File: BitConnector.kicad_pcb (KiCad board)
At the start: 2 copper layers, 21.1 x 53.3 mm, 24 parts, among them J1 JTAG, J1 disable_schmitt_trigger_action, J2 Conn_01x02, SW1 reset, U1 XC95##XL-VQ44, U2 74LVC2G14

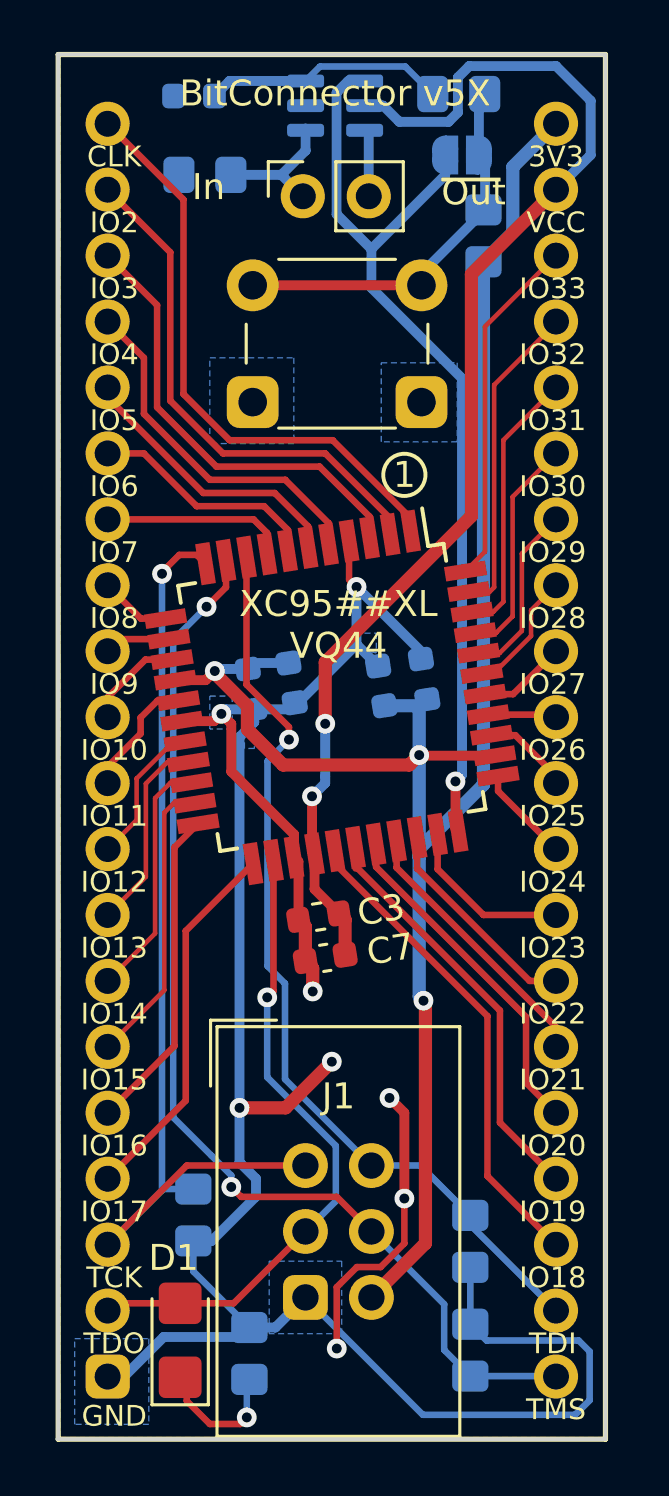
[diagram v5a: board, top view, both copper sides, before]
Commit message: Test circuit with improved GND connection connection
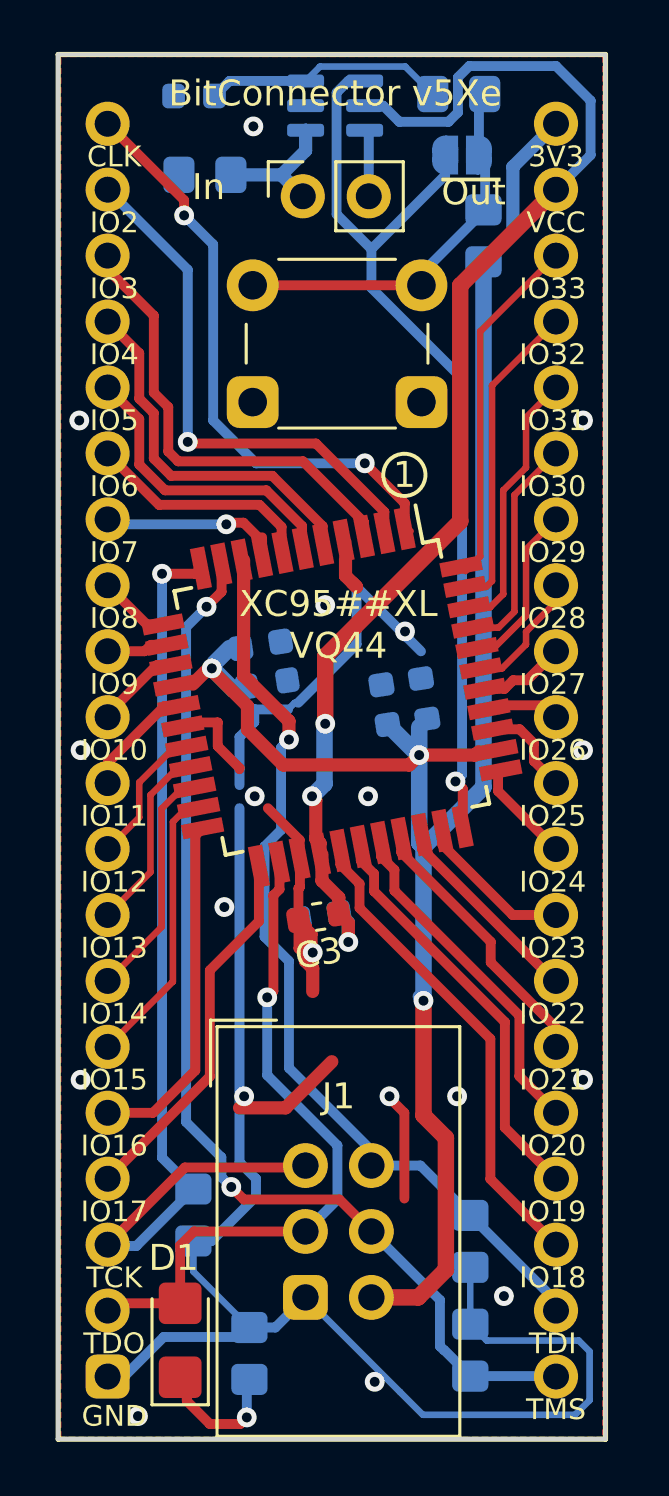
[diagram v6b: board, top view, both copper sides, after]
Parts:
- removed the G*** at (169.4, 103.2)
- added G***: LOGO, logo:logo3, B.Cu at (169.9, 104.5)
- C7: moved to B.Cu
- moved C5 1.89 mm to (167.1, 94.5), turned to 9 degrees
- moved C7 1.62 mm to (169.3, 104.9)
- moved C2 0.75 mm to (173.4, 96.6)
- moved C6 0.73 mm to (171.8, 96.8)
- moved C1 0.66 mm to (167.3, 96.0), turned to 9 degrees
- turned U1 to 281 degrees
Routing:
- net GND: track 105.7 -> 94.0 mm, vias 8 -> 19
- net /GP_IO_10: track 4.75 -> 3.33 mm
- net /JTAG_TDO: track 25.6 -> 27.0 mm
- net /GP_IO_16: track 12.6 -> 13.5 mm
- net /GP_IO_19: track 16.8 -> 15.9 mm
- net VCC: track 49.1 -> 49.9 mm, vias 2 -> 3
- net /GP_IO_20: track 13.9 -> 13.2 mm
- net /GP_IO_5: track 11.0 -> 11.6 mm
- net /GP_IO_23: track 6.63 -> 6.04 mm
- net /GP_IO_7: track 7.17 -> 7.69 mm, vias 0 -> 1
- net /GP_IO_2: track 20.1 -> 20.6 mm, vias 0 -> 1
- net /GP_IO_4: track 13.8 -> 14.3 mm
- net /CLK_GP_IO_1: vias 0 -> 2
- added copper zone on F.Cu, net GND
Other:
- board text added: "BitConnector v5Xe"
- board text removed: "BitConnector v5X"

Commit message: Optimize the distance between the two pin headers
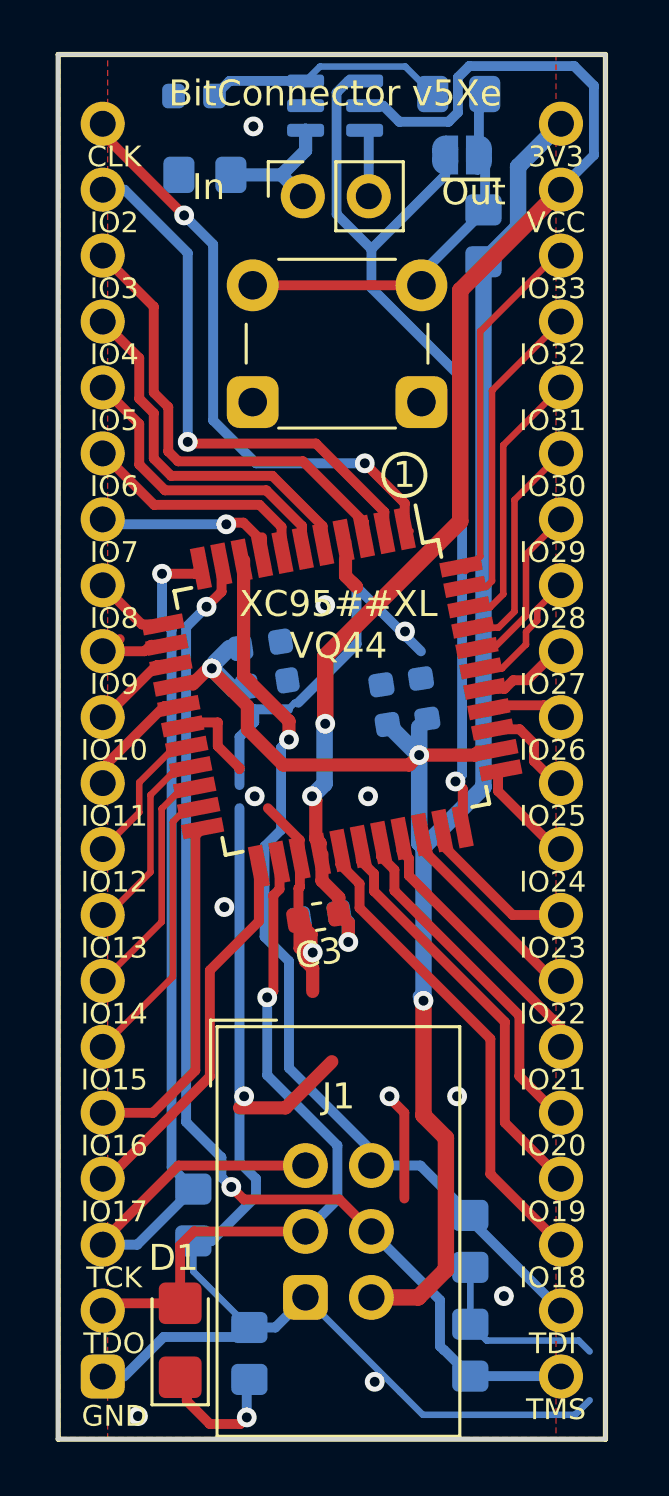
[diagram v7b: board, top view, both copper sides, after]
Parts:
- moved DIP_20_l1 0.19 mm to (161.0, 74.4)
- moved DIP_20_r1 0.19 mm to (178.6, 74.4)
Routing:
- net GND: track 94.0 -> 92.1 mm, vias 19 -> 13
- net +3V3: track 76.7 -> 75.4 mm
- net /GP_IO_28: track 4.88 -> 5.59 mm
- net /GP_IO_3: track 17.7 -> 18.3 mm
- net /JTAG_TCK: track 39.0 -> 39.6 mm
- net /GP_IO_2: track 20.6 -> 21.2 mm
- net VCC: track 49.9 -> 50.4 mm

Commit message: Revise the concept of PCB labeling
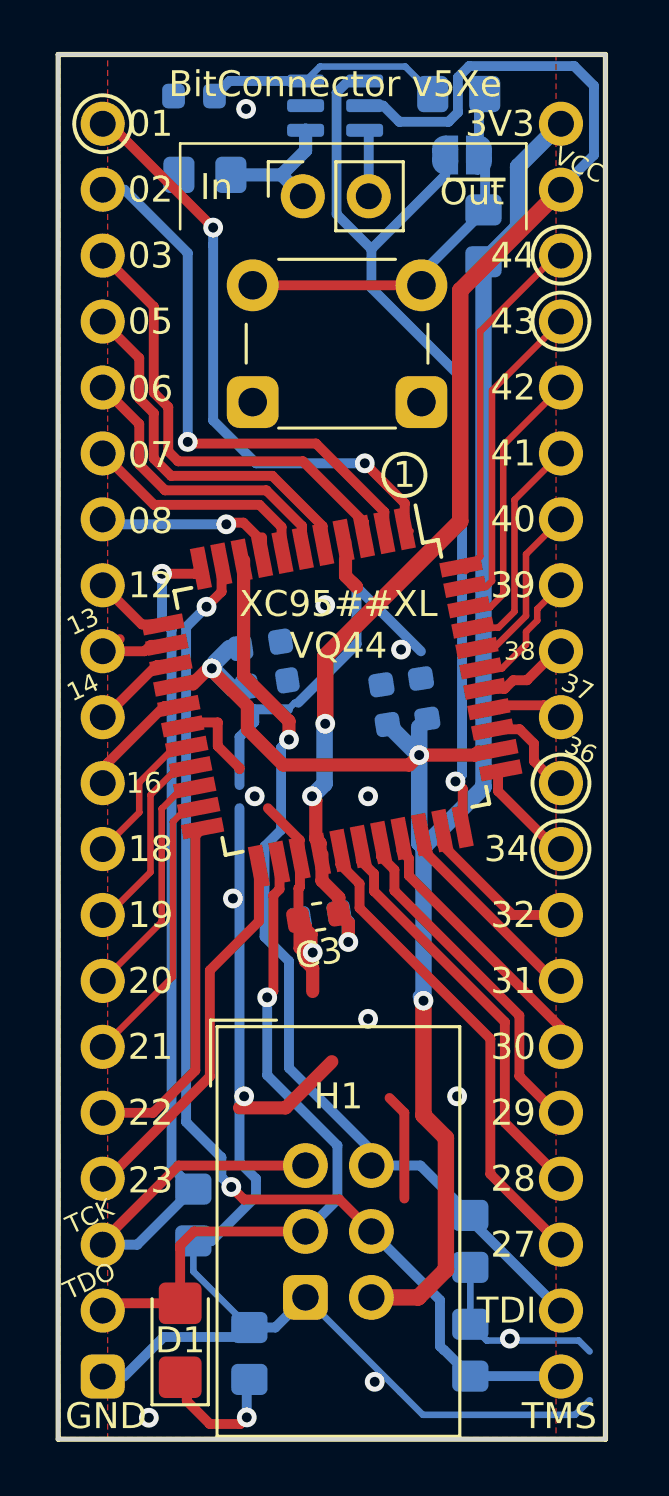
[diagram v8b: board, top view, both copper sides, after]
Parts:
- added G***: LOGO, logo:logo_mija, B.Cu at (172.1, 110.0)
- renumbered U1 to CPLD1, DIP_20_r1 to GPIO_27, J1 to H1, U2 to NOT_IC, DIP_20_l1 to PR_1, J2 to PR_3
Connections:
- net /CLK_GP_IO_1 renamed /GPIO_1GCK3
- net /GP_IO_10 renamed /GPIO_14
- net /GP_IO_11 renamed /GPIO_16
- net /GP_IO_12 renamed /GPIO_18
- net /GP_IO_13 renamed /GPIO_19
- net /GP_IO_14 renamed /GPIO_20
- net /GP_IO_15 renamed /GPIO_21
- net /GP_IO_16 renamed /GPIO_22
- net /GP_IO_17 renamed /GPIO_23
- net /GP_IO_18 renamed /GPIO_27
- net /GP_IO_19 renamed /GPIO_28
- net /GP_IO_2 renamed /GPIO_2
- net /GP_IO_20 renamed /GPIO_29
- net /GP_IO_21 renamed /GPIO_30
- net /GP_IO_22 renamed /GPIO_31
- net /GP_IO_23 renamed /GPIO_32
- net /GP_IO_24 renamed /GPIO_34GTS2
- net /GP_IO_25 renamed /GPIO_36GTS1
- net /GP_IO_26 renamed /GPIO_37
- net /GP_IO_27 renamed /GPIO_38
- net /GP_IO_28 renamed /GPIO_39
- net /GP_IO_29 renamed /GPIO_40
- net /GP_IO_3 renamed /GPIO_3
- net /GP_IO_30 renamed /GPIO_41
- net /GP_IO_31 renamed /GPIO_42
- net /GP_IO_32 renamed /GPIO_43GCK1
- net /GP_IO_33 renamed /GPIO_44GCK2
- net /GP_IO_4 renamed /GPIO_5
- net /GP_IO_5 renamed /GPIO_6
- net /GP_IO_6 renamed /GPIO_7
- net /GP_IO_7 renamed /GPIO_8
- net /GP_IO_8 renamed /GPIO_12
- net /GP_IO_9 renamed /GPIO_13
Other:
- board text added: "01"
- board text added: "02"
- board text added: "03"
- board text added: "05"
- board text added: "06"
- board text added: "07"
- board text added: "08"
- board text added: "12"
- board text added: "13"
- board text added: "14"
- board text added: "16"
- board text added: "18"
- board text added: "19"
- board text added: "20"
- board text added: "21"
- board text added: "22"
- board text added: "23"
- board text added: "27"
- board text added: "28"
- board text added: "29"
- board text added: "30"
- board text added: "31"
- board text added: "32"
- board text added: "34"
- board text added: "36"
- board text added: "37"
- board text added: "38"
- board text added: "39"
- board text added: "40"
- board text added: "41"
- board text added: "42"
- board text added: "43"
- board text added: "44"
- board text added: "Push=Pin 33"
- board text removed: "CLK"
- board text removed: "IO10"
- board text removed: "IO11"
- board text removed: "IO12"
- board text removed: "IO13"
- board text removed: "IO14"
- board text removed: "IO15"
- board text removed: "IO16"
- board text removed: "IO17"
- board text removed: "IO18"
- board text removed: "IO19"
- board text removed: "IO2"
- board text removed: "IO20"
- board text removed: "IO21"
- board text removed: "IO22"
- board text removed: "IO23"
- board text removed: "IO24"
- board text removed: "IO25"
- board text removed: "IO26"
- board text removed: "IO27"
- board text removed: "IO28"
- board text removed: "IO29"
- board text removed: "IO3"
- board text removed: "IO30"
- board text removed: "IO31"
- board text removed: "IO32"
- board text removed: "IO33"
- board text removed: "IO4"
- board text removed: "IO5"
- board text removed: "IO6"
- board text removed: "IO7"
- board text removed: "IO8"
- board text removed: "IO9"
- board text removed: "by Micha @2021"
